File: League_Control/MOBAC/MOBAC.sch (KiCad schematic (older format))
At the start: 7 parts, among them U1 NucleoF042K6

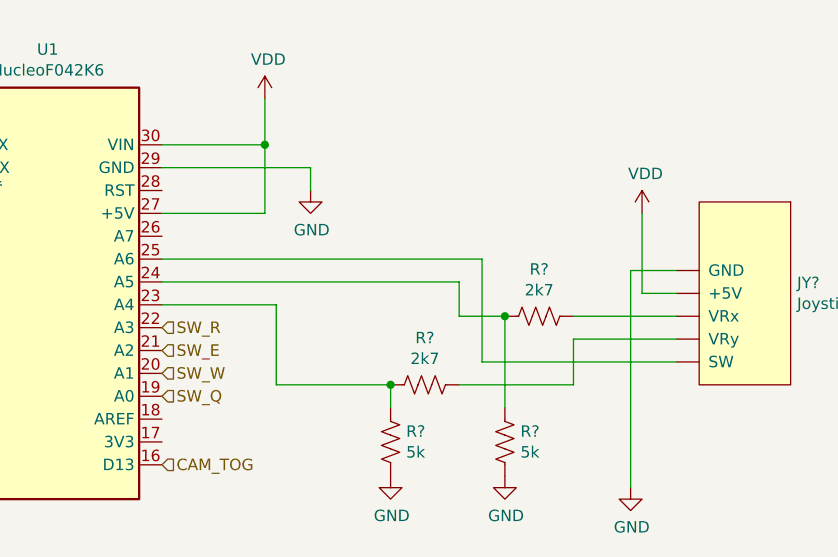
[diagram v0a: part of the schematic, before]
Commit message: Added keyboard report alongside mouse, and changed schematic to run joystick off 3.3v
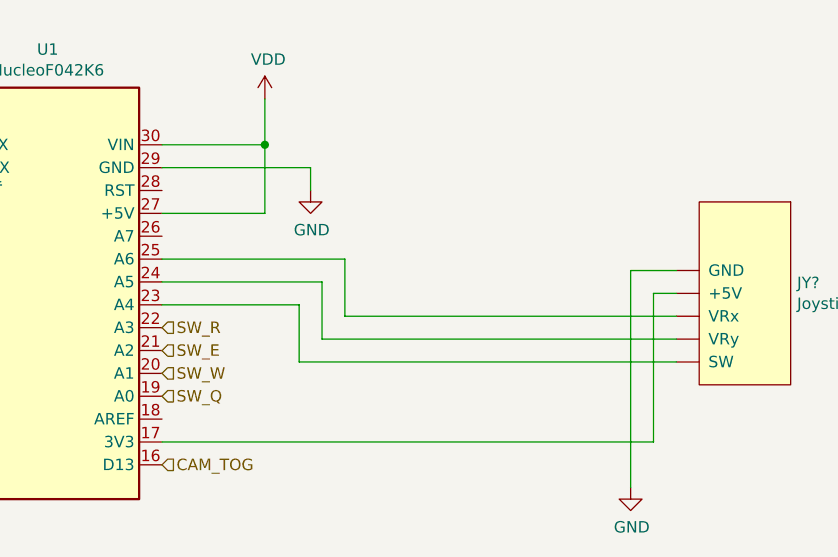
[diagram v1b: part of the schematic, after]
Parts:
- removed R? (x2): 2k7, symbol Device:R_US
- removed R? (x2): 5k, symbol Device:R_US
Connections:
- net VDD: no longer JY?.~ (VRy)
- net at U1.17 (3V3): now also JY?.~ (VRy)
- net at U1.23 (A4): now also JY?.~ (VRy)
- net at U1.24 (A5): now also JY?.~ (VRy)
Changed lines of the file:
@@
 	1    0    0    -1
 $EndComp
-Wire Wire Line
-	9300 3250 9300 4200
 $Comp
 L power:GND #PWR?
@@
 $EndComp
 Wire Wire Line
-	9500 3350 9350 3350
-Wire Wire Line
-	9350 3350 9350 3000
-$Comp
-L power:VDD #PWR?
-U 1 1 5EE921A7
-P 9350 3000
-F 0 "#PWR?" H 9350 2850 50  0001 C CNN
-F 1 "VDD" H 9365 3173 50  0000 C CNN
-F 2 "" H 9350 3000 50  0001 C CNN
-F 3 "" H 9350 3000 50  0001 C CNN
-	1    9350 3000
-	1    0    0    -1
-$EndComp
-$Comp
-L Device:R_US R?
-U 1 1 5EE95D6D
-P 8900 3450
-F 0 "R?" V 8695 3450 50  0000 C CNN
-F 1 "2k7" V 8786 3450 50  0000 C CNN
-F 2 "" V 8940 3440 50  0001 C CNN
-F 3 "~" H 8900 3450 50  0001 C CNN
-	1    8900 3450
-	0    1    1    0
-$EndComp
-Wire Wire Line
 	9300 3250 9500 3250
-$Comp
-L Device:R_US R?
-U 1 1 5EE9CF6B
-P 8400 3750
-F 0 "R?" V 8195 3750 50  0000 C CNN
-F 1 "2k7" V 8286 3750 50  0000 C CNN
-F 2 "" V 8440 3740 50  0001 C CNN
-F 3 "~" H 8400 3750 50  0001 C CNN
-	1    8400 3750
-	0    1    1    0
-$EndComp
-Wire Wire Line
-	9500 3450 9050 3450
-Wire Wire Line
-	9500 3550 9050 3550
-Wire Wire Line
-	9050 3550 9050 3750
-Wire Wire Line
-	8550 3750 9050 3750
-Wire Wire Line
-	8750 3450 8750 3850
-$Comp
-L Device:R_US R?
-U 1 1 5EEA0ACA
-P 8750 4000
-F 0 "R?" H 8818 4046 50  0000 L CNN
-F 1 "5k" H 8818 3955 50  0000 L CNN
-F 2 "" V 8790 3990 50  0001 C CNN
-F 3 "~" H 8750 4000 50  0001 C CNN
-	1    8750 4000
-	1    0    0    -1
-$EndComp
-Wire Wire Line
-	8250 3750 8250 3850
-$Comp
-L Device:R_US R?
-U 1 1 5EEA14C3
-P 8250 4000
-F 0 "R?" H 8318 4046 50  0000 L CNN
-F 1 "5k" H 8318 3955 50  0000 L CNN
-F 2 "" V 8290 3990 50  0001 C CNN
-F 3 "~" H 8250 4000 50  0001 C CNN
-	1    8250 4000
-	1    0    0    -1
-$EndComp
-$Comp
-L power:GND #PWR?
-U 1 1 5EEA1A3B
-P 8750 4150
-F 0 "#PWR?" H 8750 3900 50  0001 C CNN
-F 1 "GND" H 8755 3977 50  0000 C CNN
-F 2 "" H 8750 4150 50  0001 C CNN
-F 3 "" H 8750 4150 50  0001 C CNN
-	1    8750 4150
-	1    0    0    -1
-$EndComp
-$Comp
-L power:GND #PWR?
-U 1 1 5EEA1E13
-P 8250 4150
-F 0 "#PWR?" H 8250 3900 50  0001 C CNN
-F 1 "GND" H 8255 3977 50  0000 C CNN
-F 2 "" H 8250 4150 50  0001 C CNN
-F 3 "" H 8250 4150 50  0001 C CNN
-	1    8250 4150
-	1    0    0    -1
-$EndComp
-Wire Wire Line
-	8250 3750 7750 3750
-Connection ~ 8250 3750
-Wire Wire Line
-	7750 3750 7750 3400
-Wire Wire Line
-	7750 3400 7250 3400
-Wire Wire Line
-	8750 3450 8550 3450
-Wire Wire Line
-	8550 3450 8550 3300
-Wire Wire Line
-	8550 3300 7250 3300
-Connection ~ 8750 3450
 NoConn ~ 4950 3050
 Wire Wire Line
@@
 Wire Wire Line
 	5550 3900 6250 3900
-Wire Wire Line
-	9500 3650 8650 3650
-Wire Wire Line
-	8650 3650 8650 3200
-Wire Wire Line
-	8650 3200 7250 3200
 Text HLabel 7250 3800 2    50   Input ~ 0
 SW_Q
@@
 Text HLabel 7250 4100 2    50   Input ~ 0
 CAM_TOG
+Wire Wire Line
+	9300 3250 9300 4200
+Wire Wire Line
+	9500 3350 9400 3350
+Wire Wire Line
+	9400 3350 9400 4000
+Wire Wire Line
+	9400 4000 7250 4000
+Wire Wire Line
+	7850 3650 7850 3400
+Wire Wire Line
+	7850 3400 7250 3400
+Wire Wire Line
+	7850 3650 9500 3650
+Wire Wire Line
+	7950 3550 7950 3300
+Wire Wire Line
+	7950 3300 7250 3300
+Wire Wire Line
+	7950 3550 9500 3550
+Wire Wire Line
+	8050 3450 8050 3200
+Wire Wire Line
+	8050 3200 7250 3200
+Wire Wire Line
+	8050 3450 9500 3450
 $EndSCHEMATC

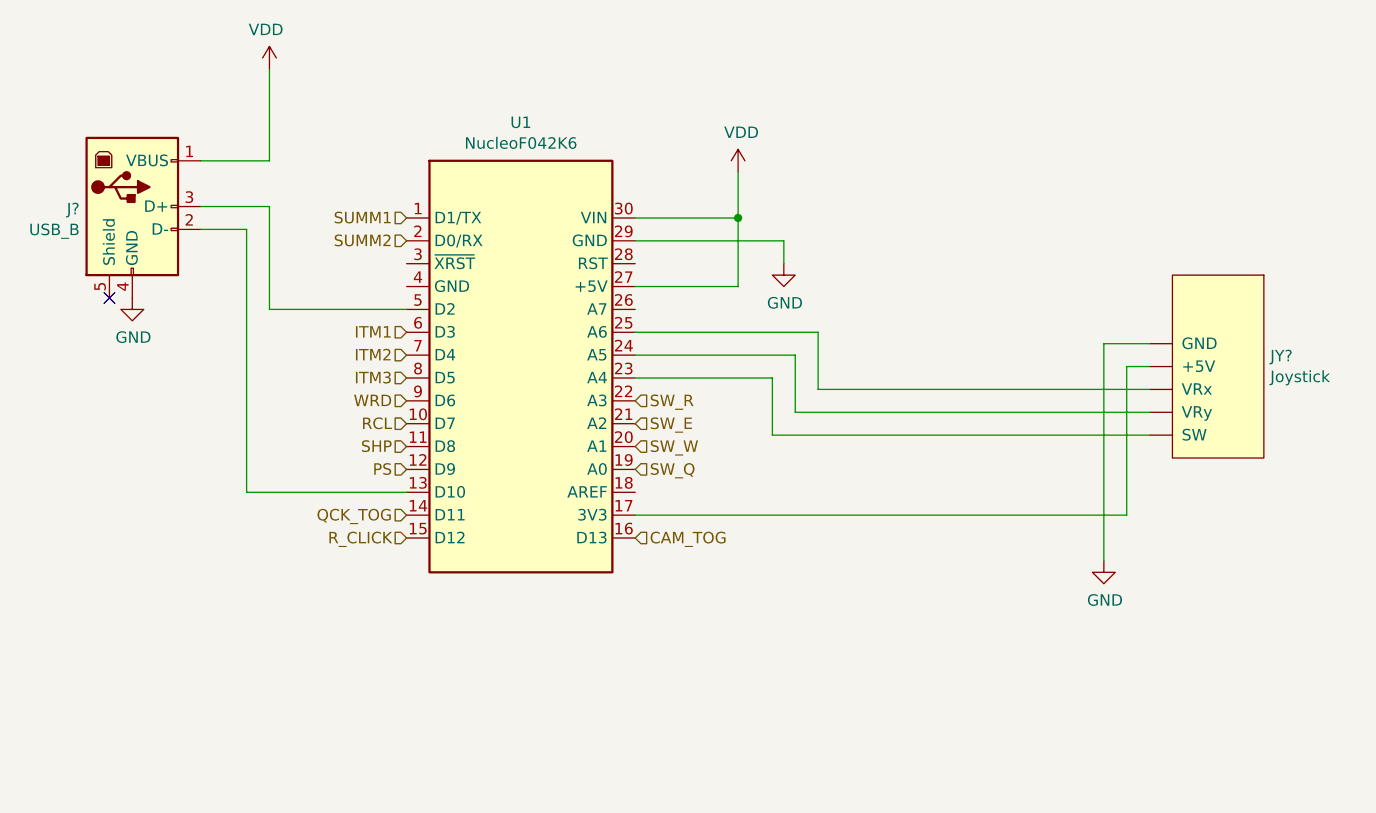
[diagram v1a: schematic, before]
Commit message: Changed the bindings to match physical hardware. Inverted joystick y.
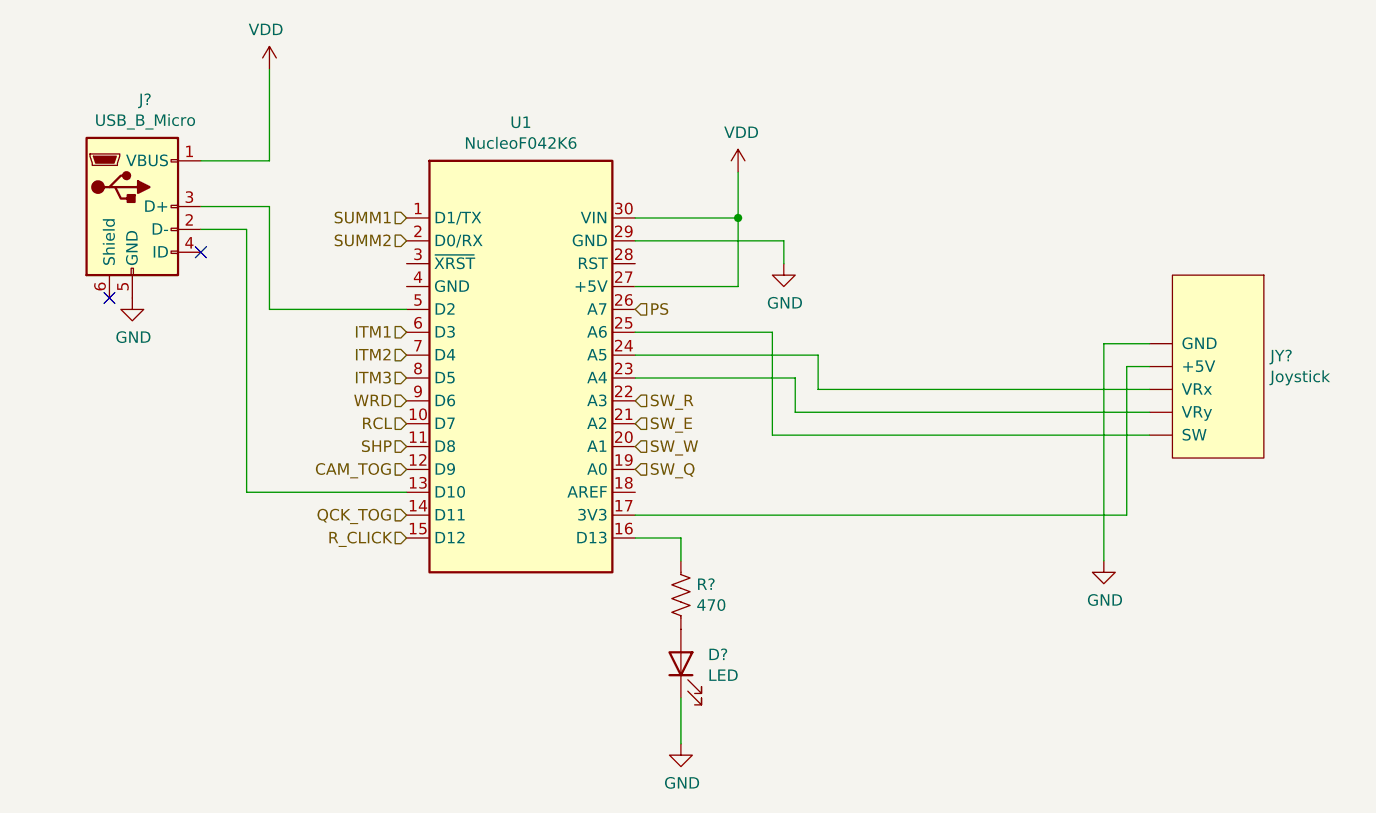
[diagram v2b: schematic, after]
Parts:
- removed J?: USB_B, symbol Connector:USB_B
- added D?: LED, symbol Device:LED
- added J?: USB_B_Micro, symbol Connector:USB_B_Micro
- added R?: 470, symbol Device:R_US
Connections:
- net CAM_TOG: now also U1.12 (D9); no longer U1.16 (D13)
- net GND: now also D?.1 (K), J?.5 (GND)
- net PS: now also U1.26 (A7); no longer U1.12 (D9)
- net VDD: now also J?.1 (VBUS)
- net at U1.13 (D10): now also J?.2 (D-)
- net at U1.5 (D2): now also J?.3 (D+)
- new net: R?.1, U1.16 (D13)
- new net: D?.2 (A), R?.2
- no-connect marks 1 -> 2
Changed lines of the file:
@@
-	1    0    0    -1
-$EndComp
-$Comp
-L Connector:USB_B J?
-U 1 1 5EE86F99
-P 5050 2650
-F 0 "J?" H 4820 2639 50  0000 R CNN
-F 1 "USB_B" H 4820 2548 50  0000 R CNN
-F 2 "" H 5200 2600 50  0001 C CNN
-F 3 " ~" H 5200 2600 50  0001 C CNN
-	1    5050 2650
 	1    0    0    -1
 $EndComp
@@
 SHP
 Text HLabel 6250 3800 0    50   Input ~ 0
-PS
+CAM_TOG
 Text HLabel 6250 4000 0    50   Input ~ 0
 QCK_TOG
 Text HLabel 6250 4100 0    50   Input ~ 0
 R_CLICK
-Text HLabel 7250 4100 2    50   Input ~ 0
-CAM_TOG
 Wire Wire Line
 	9300 3250 9300 4200
@@
 	9400 4000 7250 4000
 Wire Wire Line
-	7850 3650 7850 3400
-Wire Wire Line
-	7850 3400 7250 3400
-Wire Wire Line
 	7850 3650 9500 3650
 Wire Wire Line
-	7950 3550 7950 3300
-Wire Wire Line
-	7950 3300 7250 3300
-Wire Wire Line
 	7950 3550 9500 3550
 Wire Wire Line
-	8050 3450 8050 3200
-Wire Wire Line
-	8050 3200 7250 3200
-Wire Wire Line
 	8050 3450 9500 3450
+Text HLabel 7250 3100 2    50   Input ~ 0
+PS
+$Comp
+L Device:R_US R?
+U 1 1 5F002B19
+P 7450 4350
+F 0 "R?" H 7518 4396 50  0000 L CNN
+F 1 "470" H 7518 4305 50  0000 L CNN
+F 2 "" V 7490 4340 50  0001 C CNN
+F 3 "~" H 7450 4350 50  0001 C CNN
+	1    7450 4350
+	1    0    0    -1
+$EndComp
+Wire Wire Line
+	7250 4100 7450 4100
+Wire Wire Line
+	7450 4100 7450 4200
+$Comp
+L Device:LED D?
+U 1 1 5F004BAC
+P 7450 4650
+F 0 "D?" V 7489 4532 50  0000 R CNN
+F 1 "LED" V 7398 4532 50  0000 R CNN
+F 2 "" H 7450 4650 50  0001 C CNN
+F 3 "~" H 7450 4650 50  0001 C CNN
+	1    7450 4650
+	0    -1   -1   0
+$EndComp
+Wire Wire Line
+	7450 4800 7450 5000
+$Comp
+L power:GND #PWR?
+U 1 1 5F005C8E
+P 7450 5000
+F 0 "#PWR?" H 7450 4750 50  0001 C CNN
+F 1 "GND" H 7455 4827 50  0000 C CNN
+F 2 "" H 7450 5000 50  0001 C CNN
+F 3 "" H 7450 5000 50  0001 C CNN
+	1    7450 5000
+	1    0    0    -1
+$EndComp
+$Comp
+L Connector:USB_B_Micro J?
+U 1 1 5FB1B7B0
+P 5050 2650
+F 0 "J?" H 5107 3117 50  0000 C CNN
+F 1 "USB_B_Micro" H 5107 3026 50  0000 C CNN
+F 2 "" H 5200 2600 50  0001 C CNN
+F 3 "~" H 5200 2600 50  0001 C CNN
+	1    5050 2650
+	1    0    0    -1
+$EndComp
+NoConn ~ 5350 2850
+Wire Wire Line
+	8050 3450 8050 3300
+Wire Wire Line
+	8050 3300 7250 3300
+Wire Wire Line
+	7950 3550 7950 3400
+Wire Wire Line
+	7950 3400 7250 3400
+Wire Wire Line
+	7850 3650 7850 3200
+Wire Wire Line
+	7850 3200 7250 3200
 $EndSCHEMATC
